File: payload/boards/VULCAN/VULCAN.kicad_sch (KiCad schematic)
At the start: 62 parts, among them IC1 LT1001CS8#PBF, J1 POWER, J2 I2C, J3 Serial, J4 SPI, J5 GPIO, J6 XT60PW-M, J7 Screw_Terminal_01x06, J8 Screw_Terminal_01x06, U1 DS18B20, U2 TPS61200DRC, U4 MPXV7002DP, U5 DEV-16771, U6 MAX31850KATB+T, U7 MAX31850KATB+T, U8 MAX31850KATB+T

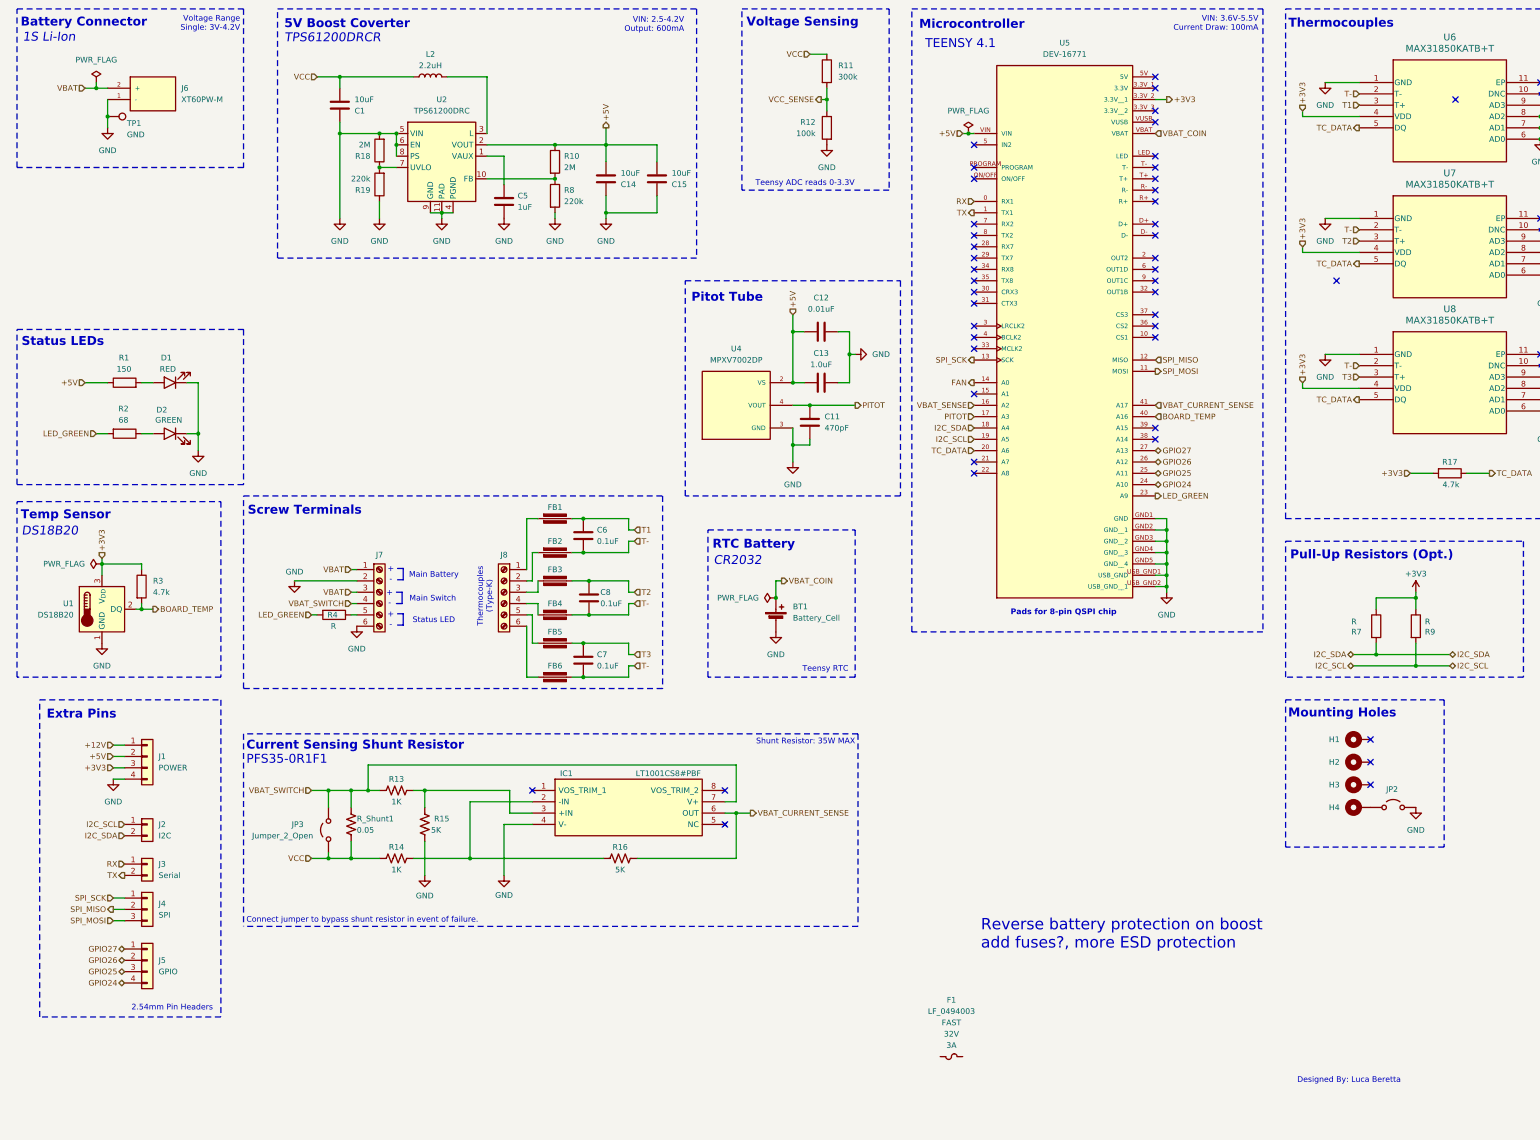
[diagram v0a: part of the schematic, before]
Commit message: reverted back to bucks
since we need weight in the form of batteries
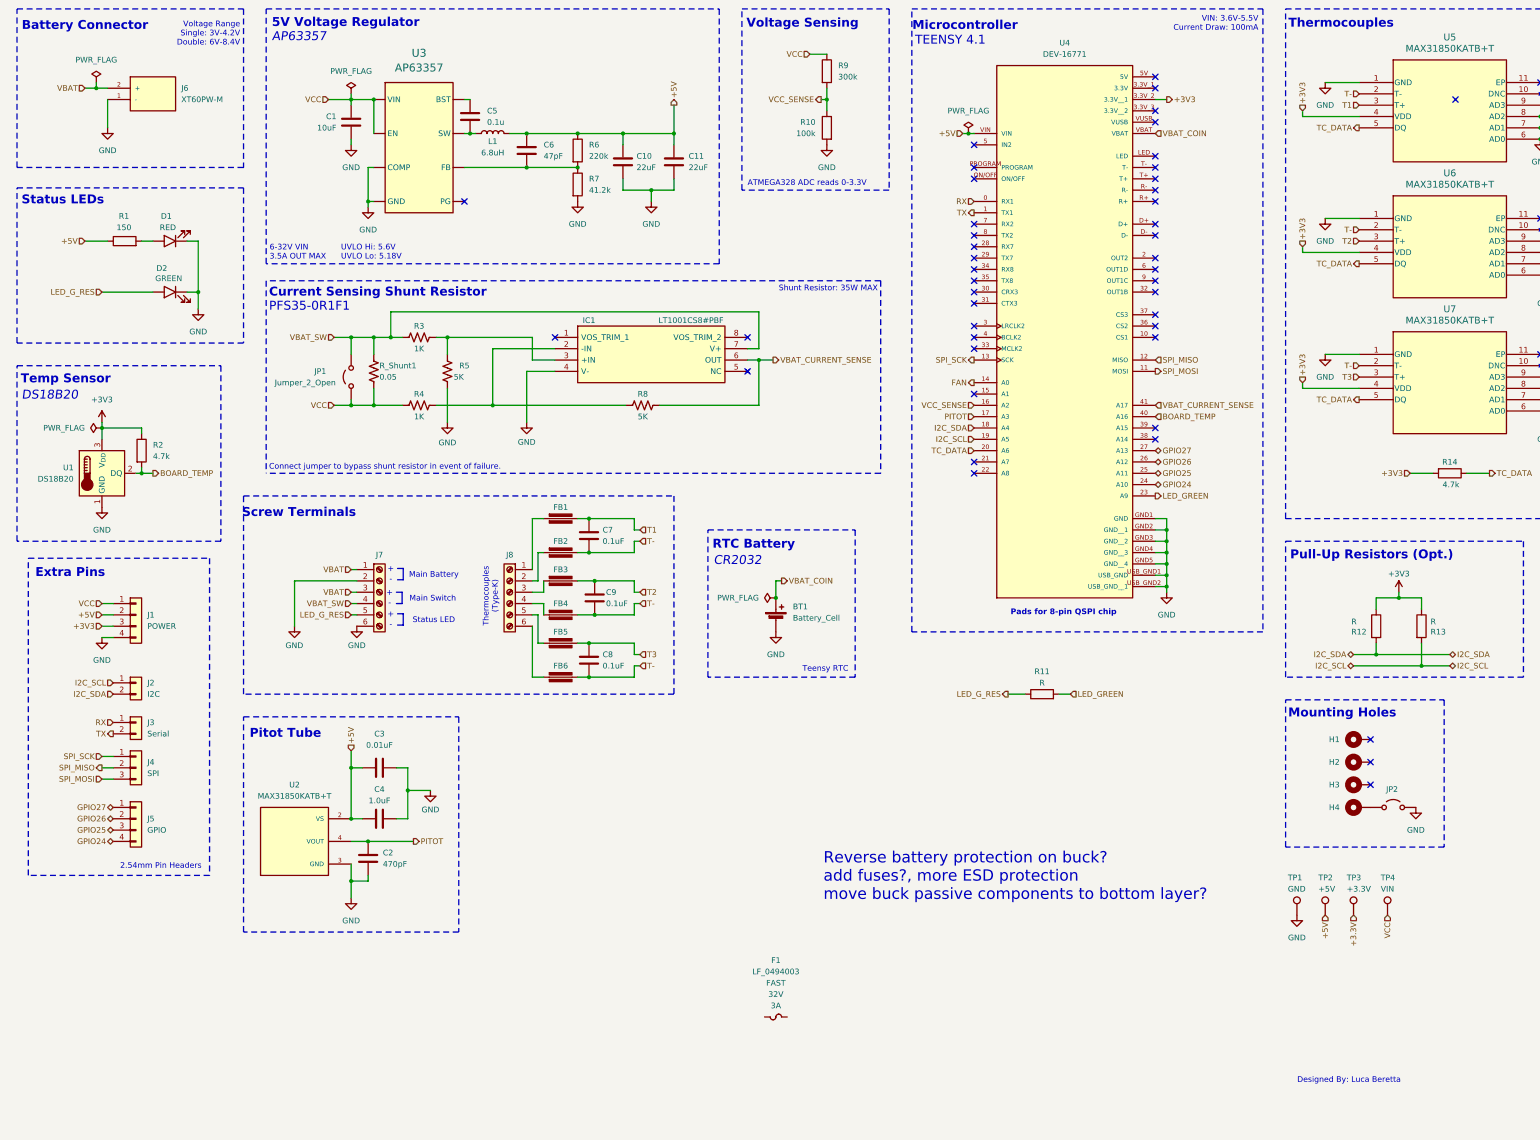
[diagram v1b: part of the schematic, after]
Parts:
- removed C14, C15: 10uF, Capacitor_SMD:C_0805_2012Metric_Pad1.18x1.45mm_HandSolder, symbol Device:C
- removed L2: 2.2uH, symbol Device:L
- removed R10, R18: 2M, Resistor_SMD:R_0805_2012Metric_Pad1.20x1.40mm_HandSolder, symbol Device:R
- removed R17: 4.7k, Resistor_SMD:R_0805_2012Metric_Pad1.20x1.40mm_HandSolder, symbol Device:R
- removed R19, R8: 220k, Resistor_SMD:R_0805_2012Metric_Pad1.20x1.40mm_HandSolder, symbol Device:R
- removed R2: 68, Resistor_SMD:R_0805_2012Metric_Pad1.20x1.40mm_HandSolder, symbol Device:R
- removed R4: R, Resistor_SMD:R_0805_2012Metric_Pad1.20x1.40mm_HandSolder, symbol Device:R
- removed U2: TPS61200DRC, Package_SON:Texas_S-PVSON-N10_ThermalVias, symbol Regulator_Switching:TPS61200DRC
- removed U8: MAX31850KATB+T, CustomFootprintLib:SON50P300X400X80-11N, symbol CustomComponents:MAX31850KATB+T
- added C10, C11: 22uF, Capacitor_SMD:C_0805_2012Metric_Pad1.18x1.45mm_HandSolder, symbol Device:C
- added C6: 47pF, Capacitor_SMD:C_0805_2012Metric_Pad1.18x1.45mm_HandSolder, symbol Device:C
- added L1: 6.8uH, CustomFootprintLib:IND_SRN8040TA-6R8M, symbol Device:L
- added R11: R, Resistor_SMD:R_0805_2012Metric_Pad1.20x1.40mm_HandSolder, symbol Device:R
- added R14: 4.7k, Resistor_SMD:R_0805_2012Metric_Pad1.20x1.40mm_HandSolder, symbol Device:R
- added R6: 220k, Resistor_SMD:R_0805_2012Metric_Pad1.20x1.40mm_HandSolder, symbol Device:R
- added R7: 41.2k, Resistor_SMD:R_0805_2012Metric_Pad1.20x1.40mm_HandSolder, symbol Device:R
- added TP2: +5V, TestPoint:TestPoint_Pad_D1.0mm, symbol Connector:TestPoint
- added TP3: +3.3V, TestPoint:TestPoint_Pad_D1.0mm, symbol Connector:TestPoint
- added TP4: VIN, TestPoint:TestPoint_Pad_D1.0mm, symbol Connector:TestPoint
- added U3: AP63357, CustomFootprintLib:AP63356 (V-DFN3020-13), symbol CustomComponents:AP63357_(SparkFun_Buck_Regulator_5V)
- added U5: MAX31850KATB+T, CustomFootprintLib:SON50P300X400X80-11N, symbol CustomComponents:MAX31850KATB+T
- C5: value 1uF -> 0.1u
- J1: footprint Connector_PinSocket_2.54mm:PinSocket_1x04_P2.54mm_Vertical -> Connector_PinSocket_2.54mm:PinSocket_1x03_P2.54mm_Vertical
- J2: footprint Connector_PinSocket_2.54mm:PinSocket_1x02_P2.54mm_Vertical -> Connector_PinSocket_2.54mm:PinSocket_1x04_P2.54mm_Vertical
- J3: footprint Connector_PinSocket_2.54mm:PinSocket_1x02_P2.54mm_Vertical -> Connector_AMASS:AMASS_XT60IPW-M_1x03_P7.20mm_Horizontal
- J4: footprint Connector_PinSocket_2.54mm:PinSocket_1x03_P2.54mm_Vertical -> CustomFootprintLib:TERMBLOCK_OSTTE060104
- J5: footprint Connector_PinSocket_2.54mm:PinSocket_1x04_P2.54mm_Vertical -> CustomFootprintLib:TERMBLOCK_OSTTE060104
- J6: footprint Connector_AMASS:AMASS_XT60IPW-M_1x03_P7.20mm_Horizontal -> Connector_PinSocket_2.54mm:PinSocket_1x04_P2.54mm_Vertical
- J7, J8: footprint CustomFootprintLib:TERMBLOCK_OSTTE060104 -> Connector_PinSocket_2.54mm:PinSocket_1x02_P2.54mm_Vertical
- U2: renamed from U4; value MPXV7002DP -> MAX31850KATB+T; footprint SnapEDA Library:XDCR_MPXV7002DP -> CustomFootprintLib:SON50P300X400X80-11N; MAXIMUM_PACKAGE_HEIGHT 9.91 mm -> (none); PARTREV 4 -> (none); Purchase https://www.digikey.com/en/products/detail/nxp-usa-inc/mpxv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 -> https://www.digikey.com/en/products/detail/analog-devices-i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
- renumbered C11 to C2, C12 to C3, C13 to C4, C6 to C7, C7 to C8, C8 to C9, JP3 to JP1, R12 to R10, R7 to R12, R9 to R13, R3 to R2, R13 to R3, R14 to R4, R15 to R5, R16 to R8, R11 to R9, U5 to U4
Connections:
- net +12V is gone; now on net VCC: J1.1 (Pin_1)
- net VBAT_SENSE is gone; now on net VCC_SENSE: U4.16 (A2)
- net +3V3: now also U6.6 (AD0), U7.7 (AD1), R14.2, U5.4 (VDD); no longer U7.6 (AD0)
- net +5V: now also C10.1, C11.1, C6.1, L1.2, R6.1, TP2.1
- net GND: now also C1.2, U7.6 (AD0), C10.2, C11.2, R7.2, U3.4 (COMP), U3.8 (GND), U5.1 (GND), U5.6 (AD0), U5.7 (AD1), U5.8 (AD2), U5.9 (AD3); no longer C1.1, C5.2, U6.6 (AD0), U7.7 (AD1)
- net LED_GREEN: now also R11.2
- net T-: now also U5.2 (T-)
- net T1: now also U5.3 (T+); no longer U6.3 (T+)
- net T2: now also U6.3 (T+); no longer U7.3 (T+)
- net T3: now also U7.3 (T+)
- net TC_DATA: now also R14.1, U5.5 (DQ)
- net VCC: now also C1.1, TP4.1, U3.1 (VIN), U3.2 (EN); no longer C1.2
- net at C5.1: now also U3.6 (BST)
- net LED_G_RES: now reaches D2.A
- net LED_G_RES: now also J7.5 (Pin_5), R11.1
- net VBAT_SWITCH renamed VBAT_SW
- new net: C5.2, L1.1, U3.9 (SW)
- new net: C6.2, R6.2, R7.1, U3.3 (FB)
- new net +3.3V: TP3.1
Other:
- note added: "5V Voltage Regulator"
- note added: "6-32V VIN 3.5A OUT MAX"
- note added: "AP63357"
- note added: "ATMEGA328 ADC reads 0-3.3V"
- note added: "Reverse battery protection on buck? add fuses?, more ESD protection move buck passive components to bottom layer?"
- note added: "UVLO Hi: 5.6V UVLO Lo: 5.18V"
- note added: "Voltage Range Single: 3V-4.2V Double: 6V-8.4V"
- note removed: "1S Li-Ion"
- note removed: "5V Boost Coverter"
- note removed: "Reverse battery protection on boost add fuses?, more ESD protection"
- note removed: "TPS61200DRCR"
- note removed: "Teensy ADC reads 0-3.3V"
- note removed: "VIN: 2.5-4.2V Output: 600mA"
- note removed: "Voltage Range Single: 3V-4.2V"
- moved on the sheet: C2, C3, C4, C7, C8, C9, D1, D2, FB1, FB2, FB3, FB4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

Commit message: updates
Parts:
- removed F1: LF_0494003, Skyhawkson_Footprints:LF_0494_(0603), symbol Skyhawkson-Miscellaneous:LF_0494003
- removed J6: XT60PW-M, Connector_PinSocket_2.54mm:PinSocket_1x04_P2.54mm_Vertical, symbol CustomComponents:XT60PW-M
- added C1: 22uF, Capacitor_SMD:C_0805_2012Metric_Pad1.18x1.45mm_HandSolder, symbol Device:C
- added C14, C15, C16: 0.1uF, Capacitor_SMD:C_0805_2012Metric_Pad1.18x1.45mm_HandSolder, symbol Device:C
- added C2: 10uF, Capacitor_SMD:C_0805_2012Metric_Pad1.18x1.45mm_HandSolder, symbol Device:C
- added D3: SPHV12-01ETG-C, PCM_Diode_SMD_Handsoldering_AKL:D_SOD-882_DFN1006-2_TVS, symbol Device:D_TVS
- added D4: BAT165A, Diode_SMD:D_SOD-323_HandSoldering, symbol PCM_Diode_Schottky_AKL:BAT165A
- added F1: 1.5A, Fuse:Fuse_0805_2012Metric_Pad1.15x1.40mm_HandSolder, symbol Device:Fuse
- added J1: XT60PW-M, CustomFootprintLib:AMASS_XT60PW-M, symbol CustomComponents:XT60PW-M
- added JP1: Jumper_2_Open, Jumper:SolderJumper-2_P1.3mm_Open_RoundedPad1.0x1.5mm, symbol Jumper:Jumper_2_Open
- added JP3, JP4, JP5: Jumper_2_Open, CustomFootprintLib:SolderJumper, symbol Jumper:Jumper_2_Open
- added U1: AZ1117IH-5.0TRG1, CustomFootprintLib:SOT223-5_DIO, symbol CustomComponents:AZ1117IH-5.0TRG1
- C10: renamed from C8; value 0.1uF -> 0.01uF
- C11: renamed from C9; value 0.1uF -> 0.01uF
- C7: renamed from C5; value 0.1u -> 0.1uF
- C9: renamed from C7; value 0.1uF -> 0.01uF
- FB1, FB2, FB3, FB4, FB5, FB6: value Ferrite_Bead -> 2508056017Y2
- J2: renamed from J1; footprint Connector_PinSocket_2.54mm:PinSocket_1x03_P2.54mm_Vertical -> Connector_PinSocket_2.54mm:PinSocket_1x04_P2.54mm_Vertical
- J3: renamed from J2; footprint Connector_PinSocket_2.54mm:PinSocket_1x04_P2.54mm_Vertical -> Connector_PinSocket_2.54mm:PinSocket_1x02_P2.54mm_Vertical
- J4: renamed from J3; footprint Connector_AMASS:AMASS_XT60IPW-M_1x03_P7.20mm_Horizontal -> Connector_PinSocket_2.54mm:PinSocket_1x02_P2.54mm_Vertical
- J5: renamed from J4; footprint CustomFootprintLib:TERMBLOCK_OSTTE060104 -> Connector_PinSocket_2.54mm:PinSocket_1x03_P2.54mm_Vertical
- J6: renamed from J5; footprint CustomFootprintLib:TERMBLOCK_OSTTE060104 -> Connector_PinSocket_2.54mm:PinSocket_1x04_P2.54mm_Vertical
- J7, J8: footprint Connector_PinSocket_2.54mm:PinSocket_1x02_P2.54mm_Vertical -> CustomFootprintLib:TERMBLOCK_OSTTE060104
- U3: renamed from U2; value MAX31850KATB+T -> MPXV7002DP; footprint CustomFootprintLib:SON50P300X400X80-11N -> SnapEDA Library:XDCR_MPXV7002DP
- renumbered C10 to C12, C11 to C13, C1 to C3, C2 to C4, C3 to C5, C4 to C6, C6 to C8, JP1 to JP2, JP2 to JP6, U1 to U2, U3 to U4, U4 to U5, U5 to U6, U6 to U7, U7 to U8
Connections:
- net +3V3: now also C14.1, C15.1, C16.1
- net +5V: now also C2.1, U1.3 (INPUT)
- net GND: now also C1.2, C14.2, C15.2, C16.2, C2.2, D3.1 (A1), J1.2 (-), JP3.2 (B), JP4.2 (B), JP5.2 (B), U1.1 (ADJ/GND)
- net VBAT: now also D3.2 (A2), F1.1, J1.1 (+); no longer J7.3 (Pin_3)
- net VCC: now also C1.1, JP1.1 (A), U1.2 (OUTPUT); no longer C3.1, U4.1 (VIN), U4.2 (EN)
- net at H1.1: now also JP3.1 (A)
- net at H2.1: now also JP4.1 (A)
- net at H3.1: now also JP5.1 (A)
- net LED_GREEN renamed LED_GRN
- net LED_G_RES renamed LED_GRN_RES
- new net: D4.2 (A), F1.2
- new net: C3.1, JP1.2 (B), U4.1 (VIN), U4.2 (EN)
- new net VBAT_RP: D4.1 (K), J7.3 (Pin_3)
- no-connect marks 48 -> 46
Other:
- note added: "!!! Do not solder components unless Buck fails !!!"
- note added: "1A IOUT MAX 15V VIN MAX 5V VOUT"
- note added: "5V Voltage Regulator (Alt.)"
- note added: "7.2V NiMH"
- note added: "AZ1117IH-5.0TRG1"
- note added: "ESD/RP Protection"
- note added: "move buck passive components to bottom layer?"
- note removed: "04/23/2024"
- note removed: "Designed By: Luca Beretta"
- note removed: "Heat Transfer Board for Perception"
- note removed: "Reverse battery protection on buck? add fuses?, more ESD protection move buck passive components to bottom layer?"
- title: (none) -> VULCAN
- moved on the sheet: C12, C13, C3, C4, C5, C6, C7, C8, D1, D2, L1, R1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

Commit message: added ESD to TCs
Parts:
- removed C10, C11: 0.01uF, Capacitor_SMD:C_0805_2012Metric_Pad1.18x1.45mm_HandSolder, symbol Device:C
- added C12, C13: 0.01uF, Capacitor_SMD:C_0805_2012Metric_Pad1.18x1.45mm_HandSolder, symbol Device:C
- added D11, D6, D7: NUP2105LT1G, Package_TO_SOT_SMD:SOT-23-3, symbol PCM_Diode_TVS_AKL:D_TVS_Bidirectional_Generic_Dual_3com
- added HS1: Heatsink, symbol Mechanical:Heatsink
- FB1, FB2, FB3, FB4, FB5, FB6: value 2508056017Y2 -> BLM21SP471BH1D
- R12, R13: value R -> 4.7k
- TP3: value +3.3V -> +3V3
- renumbered C13 to C10, C9 to C11, C12 to C9
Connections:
- net +3.3V is gone; now on net +3V3: TP3.1
- net +5V: now also C1.1, U1.2 (OUTPUT); no longer C2.1, U1.3 (INPUT)
- net GND: now also D11.3 (Com), D6.3 (Com), D7.3 (Com)
- net T-: now also C12.2, C13.2, D11.1 (A1), D6.1 (A1), D7.1 (A1)
- net T1: now also D11.2 (A2)
- net T2: now also C12.1, D6.2 (A2)
- net T3: now also C13.1, D7.2 (A2)
- net VCC: now also C2.1, U1.3 (INPUT); no longer C1.1, U1.2 (OUTPUT)
- net FAN: no longer names the net of U5.14 (A0)
- no-connect marks 46 -> 47
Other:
- note added: "2.54mm Male Pin Headers"
- note added: "Miscellaneous"
- note added: "NUP2105LT1G"
- note added: "Teensy can use INPUT_PULLUP"
- note added: "move buck passive components to bottom layer? ferrite bead from https://www.analog.com/media/en/technical-documentation/data-sheets/max31850evkit.pdf size tvs diode for TC (only need one for T-)"
- note removed: "1.0"
- note removed: "2.54mm Pin Headers"
- note removed: "move buck passive components to bottom layer?"
- moved on the sheet: C1, C11, C2, D3, D4, F1, FB1, FB2, H1, H2, H3, H4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

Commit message: updates
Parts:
- removed D11, D6, D7: NUP2105LT1G, Package_TO_SOT_SMD:SOT-23-3, symbol PCM_Diode_TVS_AKL:D_TVS_Bidirectional_Generic_Dual_3com
- removed FB1, FB2, FB3, FB4, FB5, FB6: BLM21SP471BH1D, PCM_Ferrite_SMD_AKL:Ferrite_0805_2012Metric_Pad1.05x1.20mm_BigPads, symbol PCM_Device_AKL:Ferrite_Bead
- renumbered C3 to C2, C5 to C3, C6 to C4, C4 to C5, C7 to C6, C8 to C7, C2 to C8, D2 to D1, D1 to D2, U2 to U1, U1 to U2
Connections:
- net LED_GRN_RES is gone; now on net LED_GRN: D1.A, J7.5 (Pin_5), R11.1
- net LED_GRN: no longer R11.2, U5.23 (A9)
- net T-: now also J8.2 (Pin_2), J8.4 (Pin_4), J8.6 (Pin_6)
- net T1: now also J8.1 (Pin_1)
- net T2: now also J8.3 (Pin_3)
- net T3: now also J8.5 (Pin_5)
- new net: R11.2, U5.23 (A9)
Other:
- note added: "ESD Protection ±2kV"
- note added: "Pull-Up Resistors"
- note removed: "NUP2105LT1G"
- note removed: "Pull-Up Resistors (Opt.)"
- note removed: "move buck passive components to bottom layer? ferrite bead from https://www.analog.com/media/en/technical-documentation/data-sheets/max31850evkit.pdf size tvs diode for TC (only need one for T-)"
- moved on the sheet: BT1, C11, C12, C13, C3, C4, C5, D1, D2, D3, D4, F1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

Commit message: updates
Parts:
- F1: value 1.5A -> 750mA
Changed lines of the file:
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@@
 			)
 		)
-		(property "Value" "1.5A"
+		(property "Value" "750mA"
 			(at 146.05 184.15 90)
 			(effects
